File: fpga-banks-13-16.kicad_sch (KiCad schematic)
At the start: 40 parts, among them U14 XC7A100T-FGG484, U15 Oscillator_100MHz_AMJMEFB

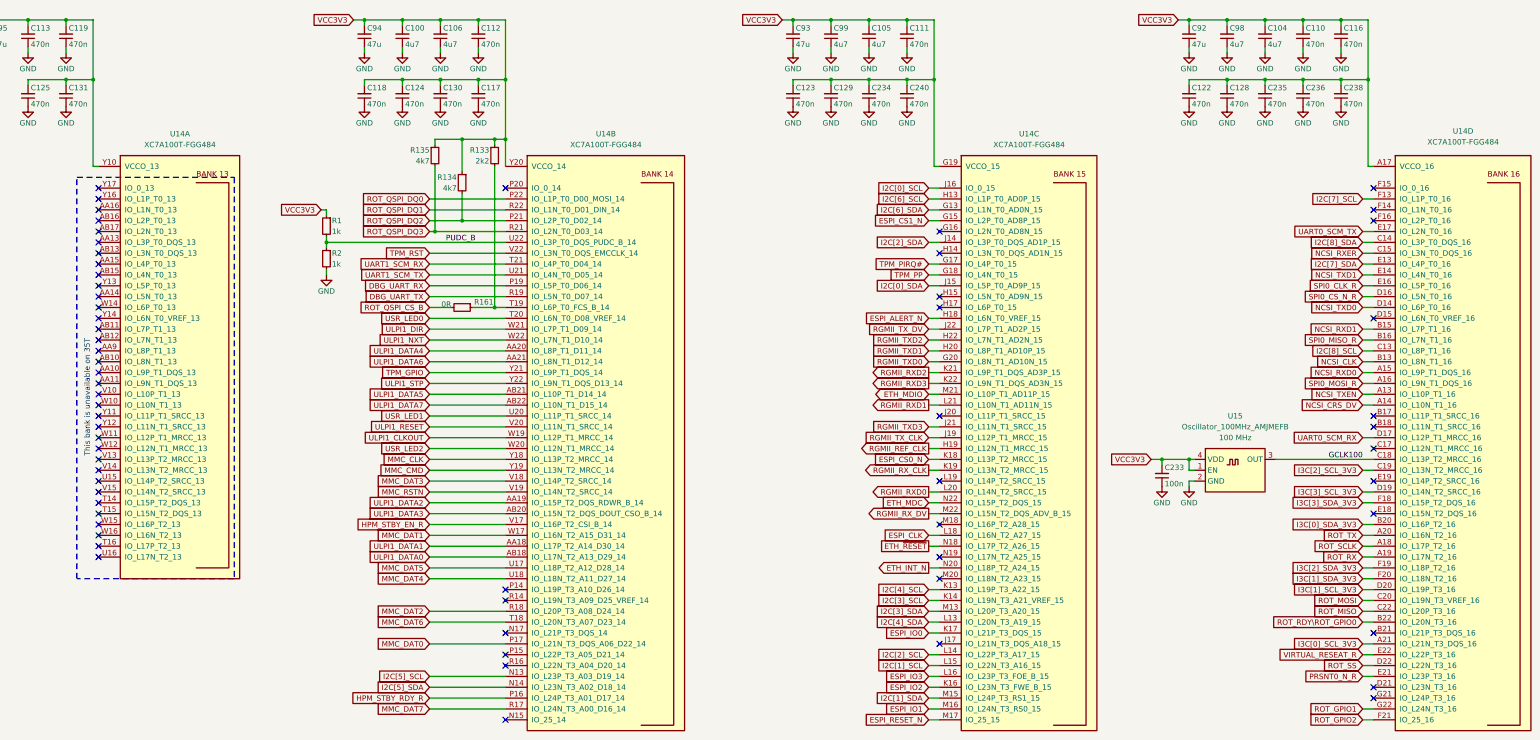
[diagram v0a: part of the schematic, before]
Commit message: [#68236] Update symbols and footprints, clean ERC and DRC
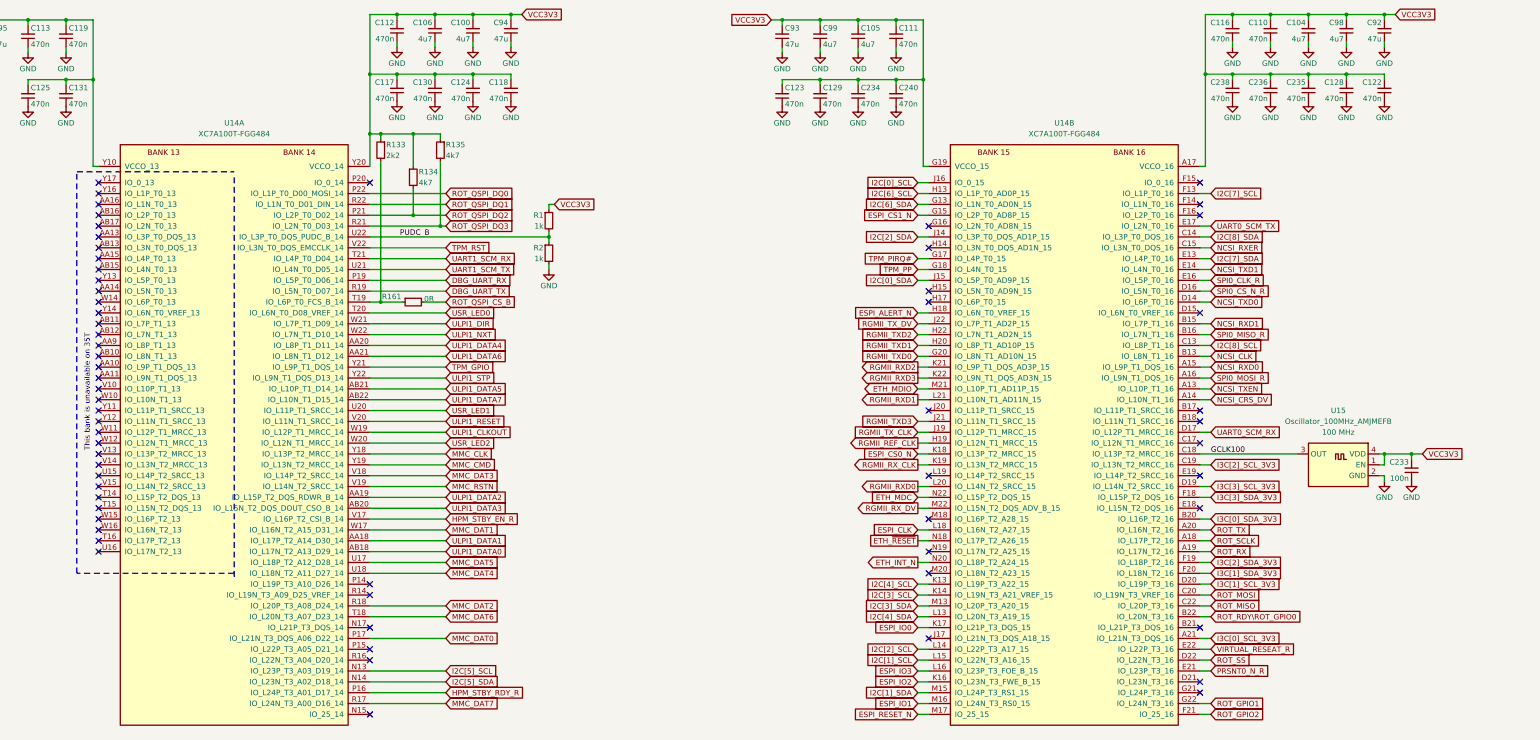
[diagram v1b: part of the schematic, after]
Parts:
- removed unit 3 of U14
- removed unit 4 of U14
- C92, C93, C94, C95: Public (none) -> False
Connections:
- net DBG_UART_RX: now also U14.P19 (IO_L5P_T0_D06_14); no longer U14.P19 (IO_L5P_T0_D06_14)
- net DBG_UART_TX: now also U14.R19 (IO_L5N_T0_D07_14); no longer U14.R19 (IO_L5N_T0_D07_14)
- net ESPI_ALERT_N: now also U14.H18 (IO_L6N_T0_VREF_15)
- net ESPI_CLK: now also U14.L18 (IO_L16N_T2_A27_15)
- net ESPI_CS0_N: now also U14.K18 (IO_L13P_T2_MRCC_15)
- net ESPI_CS1_N: now also U14.G15 (IO_L2P_T0_AD8P_15)
- net ESPI_IO0: now also U14.K17 (IO_L21P_T3_DQS_15)
- net ESPI_IO1: now also U14.M16 (IO_L24N_T3_RS0_15)
- net ESPI_IO2: now also U14.K16 (IO_L23N_T3_FWE_B_15)
- net ESPI_IO3: now also U14.L16 (IO_L23P_T3_FOE_B_15)
- net ESPI_RESET_N: now also U14.M17 (IO_25_15)
- net ETH_INT_N: now also U14.N20 (IO_L18P_T2_A24_15)
- net ETH_MDC: now also U14.N22 (IO_L15P_T2_DQS_15)
- net ETH_MDIO: now also U14.M21 (IO_L10P_T1_AD11P_15)
- net ETH_~{RESET}: now also U14.N18 (IO_L17P_T2_A26_15)
- net GCLK100: now also U14.C18 (IO_L13P_T2_MRCC_16)
- net HPM_STBY_EN_R: now also U14.V17 (IO_L16P_T2_CSI_B_14); no longer U14.V17 (IO_L16P_T2_CSI_B_14)
- net HPM_STBY_RDY_R: now also U14.P16 (IO_L24P_T3_A01_D17_14); no longer U14.P16 (IO_L24P_T3_A01_D17_14)
- net I2C[0]_SCL: now also U14.J16 (IO_0_15)
- net I2C[0]_SDA: now also U14.J15 (IO_L5P_T0_AD9P_15)
- net I2C[1]_SCL: now also U14.L15 (IO_L22N_T3_A16_15)
- net I2C[1]_SDA: now also U14.M15 (IO_L24P_T3_RS1_15)
- net I2C[2]_SCL: now also U14.L14 (IO_L22P_T3_A17_15)
- net I2C[2]_SDA: now also U14.J14 (IO_L3P_T0_DQS_AD1P_15)
- net I2C[3]_SCL: now also U14.K14 (IO_L19N_T3_A21_VREF_15)
- net I2C[3]_SDA: now also U14.M13 (IO_L20P_T3_A20_15)
- net I2C[4]_SCL: now also U14.K13 (IO_L19P_T3_A22_15)
- net I2C[4]_SDA: now also U14.L13 (IO_L20N_T3_A19_15)
- net I2C[5]_SCL: now also U14.N13 (IO_L23P_T3_A03_D19_14); no longer U14.N13 (IO_L23P_T3_A03_D19_14)
- net I2C[5]_SDA: now also U14.N14 (IO_L23N_T3_A02_D18_14); no longer U14.N14 (IO_L23N_T3_A02_D18_14)
- net I2C[6]_SCL: now also U14.H13 (IO_L1P_T0_AD0P_15)
- net I2C[6]_SDA: now also U14.G13 (IO_L1N_T0_AD0N_15)
- net I2C[7]_SCL: now also U14.F13 (IO_L1P_T0_16)
- net I2C[7]_SDA: now also U14.E13 (IO_L4P_T0_16)
- net I2C[8]_SCL: now also U14.C13 (IO_L8P_T1_16)
- net I2C[8]_SDA: now also U14.C14 (IO_L3P_T0_DQS_16)
- net I3C[0]_SCL_3V3: now also U14.A21 (IO_L21N_T3_DQS_16)
- net I3C[0]_SDA_3V3: now also U14.B20 (IO_L16P_T2_16)
- net I3C[1]_SCL_3V3: now also U14.D20 (IO_L19P_T3_16)
- net I3C[1]_SDA_3V3: now also U14.F20 (IO_L18N_T2_16)
- net I3C[2]_SCL_3V3: now also U14.C19 (IO_L13N_T2_MRCC_16)
- net I3C[2]_SDA_3V3: now also U14.F19 (IO_L18P_T2_16)
- net I3C[3]_SCL_3V3: now also U14.D19 (IO_L14N_T2_SRCC_16)
- net I3C[3]_SDA_3V3: now also U14.F18 (IO_L15P_T2_DQS_16)
- net MMC_CLK: now also U14.Y18 (IO_L13P_T2_MRCC_14); no longer U14.Y18 (IO_L13P_T2_MRCC_14)
- net MMC_CMD: now also U14.Y19 (IO_L13N_T2_MRCC_14); no longer U14.Y19 (IO_L13N_T2_MRCC_14)
- net MMC_DAT0: now also U14.P17 (IO_L21N_T3_DQS_A06_D22_14); no longer U14.P17 (IO_L21N_T3_DQS_A06_D22_14)
- net MMC_DAT1: now also U14.W17 (IO_L16N_T2_A15_D31_14); no longer U14.W17 (IO_L16N_T2_A15_D31_14)
- net MMC_DAT2: now also U14.R18 (IO_L20P_T3_A08_D24_14); no longer U14.R18 (IO_L20P_T3_A08_D24_14)
- net MMC_DAT3: now also U14.V18 (IO_L14P_T2_SRCC_14); no longer U14.V18 (IO_L14P_T2_SRCC_14)
- net MMC_DAT4: now also U14.U18 (IO_L18N_T2_A11_D27_14); no longer U14.U18 (IO_L18N_T2_A11_D27_14)
- net MMC_DAT5: now also U14.U17 (IO_L18P_T2_A12_D28_14); no longer U14.U17 (IO_L18P_T2_A12_D28_14)
- net MMC_DAT6: now also U14.T18 (IO_L20N_T3_A07_D23_14); no longer U14.T18 (IO_L20N_T3_A07_D23_14)
- net MMC_DAT7: now also U14.R17 (IO_L24N_T3_A00_D16_14); no longer U14.R17 (IO_L24N_T3_A00_D16_14)
- net MMC_RSTN: now also U14.V19 (IO_L14N_T2_SRCC_14); no longer U14.V19 (IO_L14N_T2_SRCC_14)
- net NCSI_CLK: now also U14.B13 (IO_L8N_T1_16)
- net NCSI_CRS_DV: now also U14.A14 (IO_L10N_T1_16)
- net NCSI_RXD0: now also U14.A15 (IO_L9P_T1_DQS_16)
- net NCSI_RXD1: now also U14.B15 (IO_L7P_T1_16)
- net NCSI_RXER: now also U14.C15 (IO_L3N_T0_DQS_16)
- net NCSI_TXD0: now also U14.D14 (IO_L6P_T0_16)
- net NCSI_TXD1: now also U14.E14 (IO_L4N_T0_16)
- net NCSI_TXEN: now also U14.A13 (IO_L10P_T1_16)
- net PRSNT0_N_R: now also U14.E21 (IO_L23P_T3_16)
- net PUDC_B: now also U14.U22 (IO_L3P_T0_DQS_PUDC_B_14); no longer U14.U22 (IO_L3P_T0_DQS_PUDC_B_14)
- net RGMII_REF_CLK: now also U14.H19 (IO_L12N_T1_MRCC_15)
- net RGMII_RXD0: now also U14.L20 (IO_L14N_T2_SRCC_15)
- net RGMII_RXD1: now also U14.L21 (IO_L10N_T1_AD11N_15)
- net RGMII_RXD2: now also U14.K21 (IO_L9P_T1_DQS_AD3P_15)
- net RGMII_RXD3: now also U14.K22 (IO_L9N_T1_DQS_AD3N_15)
- net RGMII_RX_CLK: now also U14.K19 (IO_L13N_T2_MRCC_15)
- net RGMII_RX_DV: now also U14.M22 (IO_L15N_T2_DQS_ADV_B_15)
- net RGMII_TXD0: now also U14.G20 (IO_L8N_T1_AD10N_15)
- net RGMII_TXD1: now also U14.H20 (IO_L8P_T1_AD10P_15)
- net RGMII_TXD2: now also U14.H22 (IO_L7N_T1_AD2N_15)
- net RGMII_TXD3: now also U14.J21 (IO_L11N_T1_SRCC_15)
- net RGMII_TX_CLK: now also U14.J19 (IO_L12P_T1_MRCC_15)
- net RGMII_TX_DV: now also U14.J22 (IO_L7P_T1_AD2P_15)
- net ROT_GPIO1: now also U14.G22 (IO_L24N_T3_16)
- net ROT_GPIO2: now also U14.F21 (IO_25_16)
- net ROT_MISO: now also U14.C22 (IO_L20P_T3_16)
- net ROT_MOSI: now also U14.C20 (IO_L19N_T3_VREF_16)
- net ROT_QSPI_DQ0: now also U14.P22 (IO_L1P_T0_D00_MOSI_14); no longer U14.P22 (IO_L1P_T0_D00_MOSI_14)
- net ROT_QSPI_DQ1: now also U14.R22 (IO_L1N_T0_D01_DIN_14); no longer U14.R22 (IO_L1N_T0_D01_DIN_14)
- net ROT_QSPI_DQ2: now also U14.P21 (IO_L2P_T0_D02_14); no longer U14.P21 (IO_L2P_T0_D02_14)
- net ROT_QSPI_DQ3: now also U14.R21 (IO_L2N_T0_D03_14); no longer U14.R21 (IO_L2N_T0_D03_14)
- net ROT_RDY\ROT_GPIO0: now also U14.B22 (IO_L20N_T3_16)
- net ROT_RX: now also U14.A19 (IO_L17N_T2_16)
- net ROT_SCLK: now also U14.A18 (IO_L17P_T2_16)
- net ROT_SS: now also U14.D22 (IO_L22N_T3_16)
- net ROT_TX: now also U14.A20 (IO_L16N_T2_16)
- net SPI0_CLK_R: now also U14.E16 (IO_L5P_T0_16)
- net SPI0_CS_N_R: now also U14.D16 (IO_L5N_T0_16)
- net SPI0_MISO_R: now also U14.B16 (IO_L7N_T1_16)
- net SPI0_MOSI_R: now also U14.A16 (IO_L9N_T1_DQS_16)
- net TPM_GPIO: now also U14.Y21 (IO_L9P_T1_DQS_14); no longer U14.Y21 (IO_L9P_T1_DQS_14)
- net TPM_PIRQ#: now also U14.G17 (IO_L4P_T0_15)
- net TPM_PP: now also U14.G18 (IO_L4N_T0_15)
- net TPM_RST: now also U14.V22 (IO_L3N_T0_DQS_EMCCLK_14); no longer U14.V22 (IO_L3N_T0_DQS_EMCCLK_14)
- net UART0_SCM_RX: now also U14.D17 (IO_L12P_T1_MRCC_16)
- net UART0_SCM_TX: now also U14.E17 (IO_L2N_T0_16)
- net UART1_SCM_RX: now also U14.T21 (IO_L4P_T0_D04_14); no longer U14.T21 (IO_L4P_T0_D04_14)
- net UART1_SCM_TX: now also U14.U21 (IO_L4N_T0_D05_14); no longer U14.U21 (IO_L4N_T0_D05_14)
- net ULPI1_CLKOUT: now also U14.W19 (IO_L12P_T1_MRCC_14); no longer U14.W19 (IO_L12P_T1_MRCC_14)
- net ULPI1_DATA0: now also U14.AB18 (IO_L17N_T2_A13_D29_14); no longer U14.AB18 (IO_L17N_T2_A13_D29_14)
- net ULPI1_DATA1: now also U14.AA18 (IO_L17P_T2_A14_D30_14); no longer U14.AA18 (IO_L17P_T2_A14_D30_14)
- net ULPI1_DATA2: now also U14.AA19 (IO_L15P_T2_DQS_RDWR_B_14); no longer U14.AA19 (IO_L15P_T2_DQS_RDWR_B_14)
- net ULPI1_DATA3: now also U14.AB20 (IO_L15N_T2_DQS_DOUT_CSO_B_14); no longer U14.AB20 (IO_L15N_T2_DQS_DOUT_CSO_B_14)
- net ULPI1_DATA4: now also U14.AA20 (IO_L8P_T1_D11_14); no longer U14.AA20 (IO_L8P_T1_D11_14)
- net ULPI1_DATA5: now also U14.AB21 (IO_L10P_T1_D14_14); no longer U14.AB21 (IO_L10P_T1_D14_14)
- net ULPI1_DATA6: now also U14.AA21 (IO_L8N_T1_D12_14); no longer U14.AA21 (IO_L8N_T1_D12_14)
- net ULPI1_DATA7: now also U14.AB22 (IO_L10N_T1_D15_14); no longer U14.AB22 (IO_L10N_T1_D15_14)
- net ULPI1_DIR: now also U14.W21 (IO_L7P_T1_D09_14); no longer U14.W21 (IO_L7P_T1_D09_14)
- net ULPI1_NXT: now also U14.W22 (IO_L7N_T1_D10_14); no longer U14.W22 (IO_L7N_T1_D10_14)
- net ULPI1_RESET: now also U14.V20 (IO_L11N_T1_SRCC_14); no longer U14.V20 (IO_L11N_T1_SRCC_14)
- net ULPI1_STP: now also U14.Y22 (IO_L9N_T1_DQS_D13_14); no longer U14.Y22 (IO_L9N_T1_DQS_D13_14)
- net USR_LED0: now also U14.T20 (IO_L6N_T0_D08_VREF_14); no longer U14.T20 (IO_L6N_T0_D08_VREF_14)
- net USR_LED1: now also U14.U20 (IO_L11P_T1_SRCC_14); no longer U14.U20 (IO_L11P_T1_SRCC_14)
- net USR_LED2: now also U14.W20 (IO_L12N_T1_MRCC_14); no longer U14.W20 (IO_L12N_T1_MRCC_14)
- net VCC3V3: now also U14.A17 (VCCO_16), U14.B14 (VCCO_16), U14.C21 (VCCO_16), U14.D18 (VCCO_16), U14.E15 (VCCO_16), U14.F22 (VCCO_16), U14.G19 (VCCO_15), U14.H16 (VCCO_15), U14.J13 (VCCO_15), U14.K20 (VCCO_15), U14.L17 (VCCO_15), U14.M14 (VCCO_14), U14.N21 (VCCO_15), U14.P18 (VCCO_14), U14.R15 (VCCO_14), U14.T22 (VCCO_14), U14.U19 (VCCO_14), U14.Y20 (VCCO_14); no longer U14.M14 (VCCO_14), U14.P18 (VCCO_14), U14.R15 (VCCO_14), U14.T22 (VCCO_14), U14.U19 (VCCO_14), U14.Y20 (VCCO_14)
- net VIRTUAL_RESEAT_R: now also U14.E22 (IO_L22P_T3_16)
- net at R133.2, R161.1: now also U14.T19 (IO_L6P_T0_FCS_B_14); no longer U14.T19 (IO_L6P_T0_FCS_B_14)
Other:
- moved on the sheet: C105, C111, C123, C129, C234, C240, C93, C99

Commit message: pcb layout progress
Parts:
- added R204, R205, R206, R207, R208, R209: 33, Resistor_SMD:R_0402_1005Metric, symbol Device:R_Small
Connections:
- net RGMII_RXD0: now also R208.1; no longer U14.L20 (IO_L14N_T2_SRCC_15)
- net RGMII_RXD1: now also R206.1; no longer U14.L21 (IO_L10N_T1_AD11N_15)
- net RGMII_RXD2: now also R204.1; no longer U14.K21 (IO_L9P_T1_DQS_AD3P_15)
- net RGMII_RXD3: now also R205.1; no longer U14.K22 (IO_L9N_T1_DQS_AD3N_15)
- net RGMII_RX_CLK: now also R207.1; no longer U14.K19 (IO_L13N_T2_MRCC_15)
- net RGMII_RX_DV: now also R209.1; no longer U14.M22 (IO_L15N_T2_DQS_ADV_B_15)
- new net RGMII_CLK_FPGA: R207.2, U14.K19 (IO_L13N_T2_MRCC_15)
- new net RGMII_RXD0_FPGA: R208.2, U14.L20 (IO_L14N_T2_SRCC_15)
- new net RGMII_RXD1_FPGA: R206.2, U14.L21 (IO_L10N_T1_AD11N_15)
- new net RGMII_RXD2_FPGA: R204.2, U14.K21 (IO_L9P_T1_DQS_AD3P_15)
- new net RGMII_RXD3_FPGA: R205.2, U14.K22 (IO_L9N_T1_DQS_AD3N_15)
- new net RGMII_RX_DV_FPGA: R209.2, U14.M22 (IO_L15N_T2_DQS_ADV_B_15)

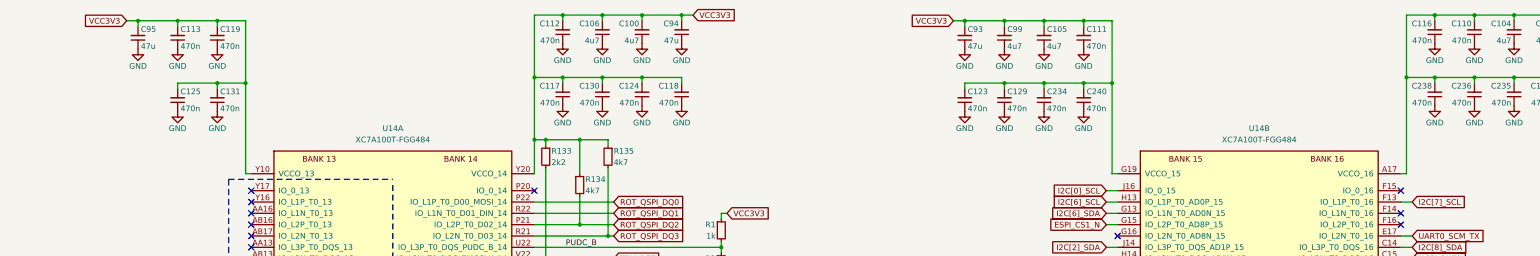
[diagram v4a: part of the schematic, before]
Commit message: a lot of routing and almost all caps of the fpga are placed down
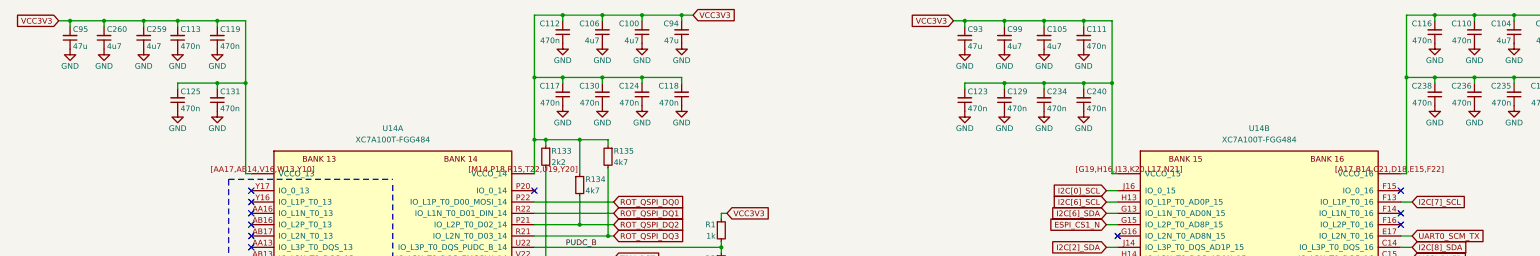
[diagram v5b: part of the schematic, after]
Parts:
- added C259, C260: C_4u7_0603, Capacitor_SMD:C_0603_1608Metric, symbol antmicroCapacitors0603:C_4u7_0603
- C100, C104, C105, C106, C98, C99: footprint antmicro-footprints:C_0603_1608Metric -> Capacitor_SMD:C_0603_1608Metric; MPN C1608X5R1V475M080AC -> C0603C475K9PAC; Manufacturer TDK -> KEMET
- C110, C111, C112, C113, C116, C117, C118, C119, C122, C123, C124, C125, C128, C129, C130, C131, C233, C234, C235, C236, C238, C240: footprint antmicro-footprints:C_0402_1005Metric -> Capacitor_SMD:C_0402_1005Metric
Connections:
- net GND: now also C259.1, C260.1
- net VCC3V3: now also U14.[A17,B14,C21,D18,E15,F22] (VCCO_16), U14.[AA17,AB14,V16,W13,Y10] (VCCO_13), U14.[G19,H16,J13,K20,L17,N21] (VCCO_15), U14.[M14,P18,R15,T22,U19,Y20] (VCCO_14), C259.2, C260.2; no longer U14.A17 (VCCO_16), U14.AA17 (VCCO_13), U14.AB14 (VCCO_13), U14.B14 (VCCO_16), U14.C21 (VCCO_16), U14.D18 (VCCO_16), U14.E15 (VCCO_16), U14.F22 (VCCO_16), U14.G19 (VCCO_15), U14.H16 (VCCO_15), U14.J13 (VCCO_15), U14.K20 (VCCO_15), U14.L17 (VCCO_15), U14.M14 (VCCO_14), U14.N21 (VCCO_15), U14.P18 (VCCO_14), U14.R15 (VCCO_14), U14.T22 (VCCO_14), U14.U19 (VCCO_14), U14.V16 (VCCO_13), U14.W13 (VCCO_13), U14.Y10 (VCCO_13), U14.Y20 (VCCO_14)
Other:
- moved on the sheet: C95, U14A

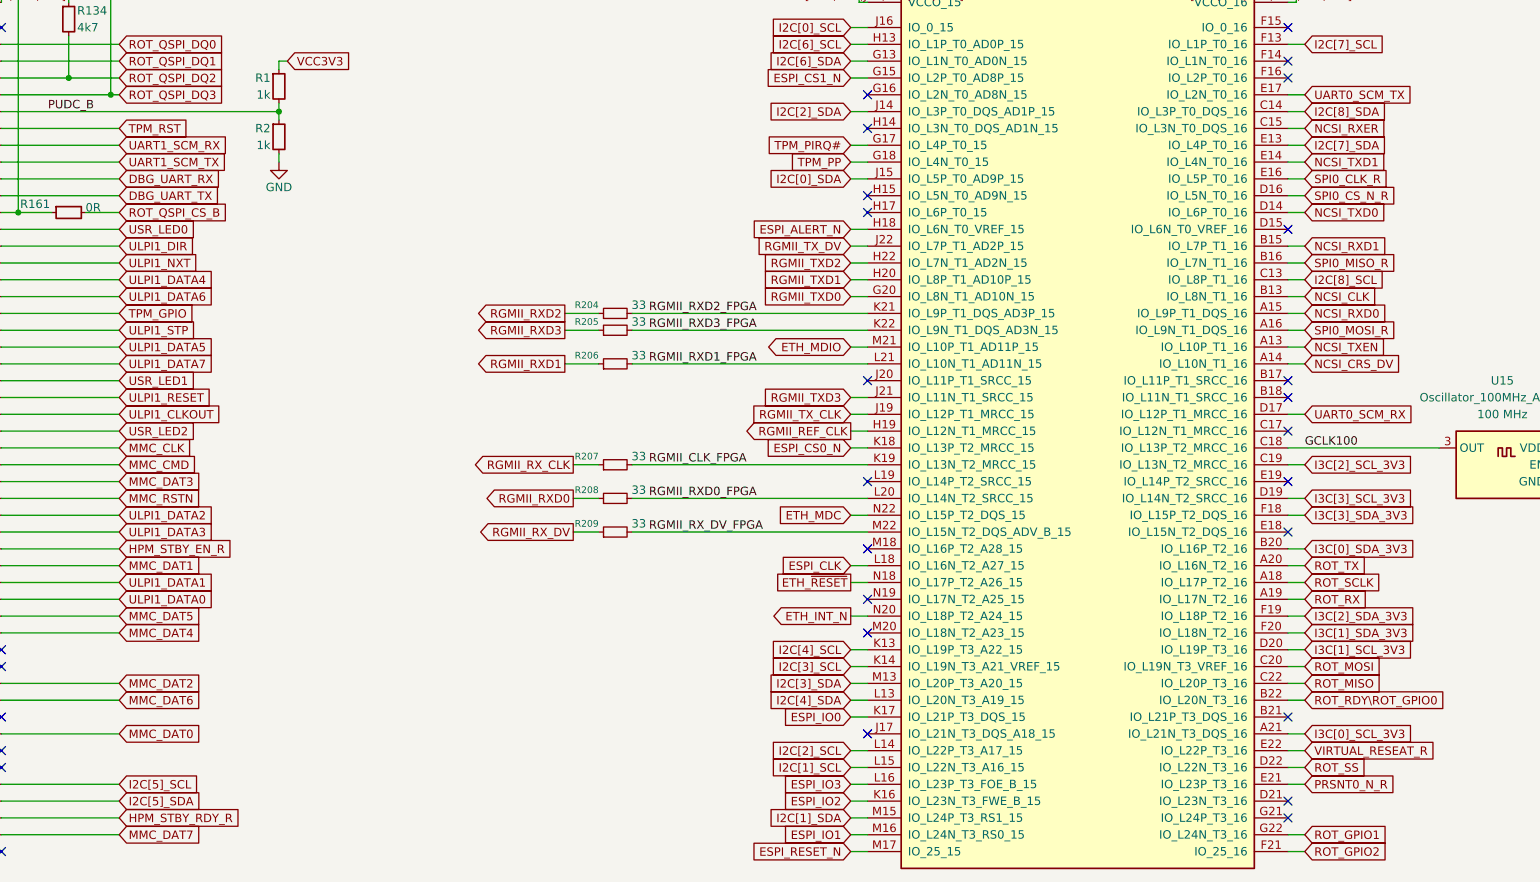
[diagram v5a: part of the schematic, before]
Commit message: a lot of poin swaps
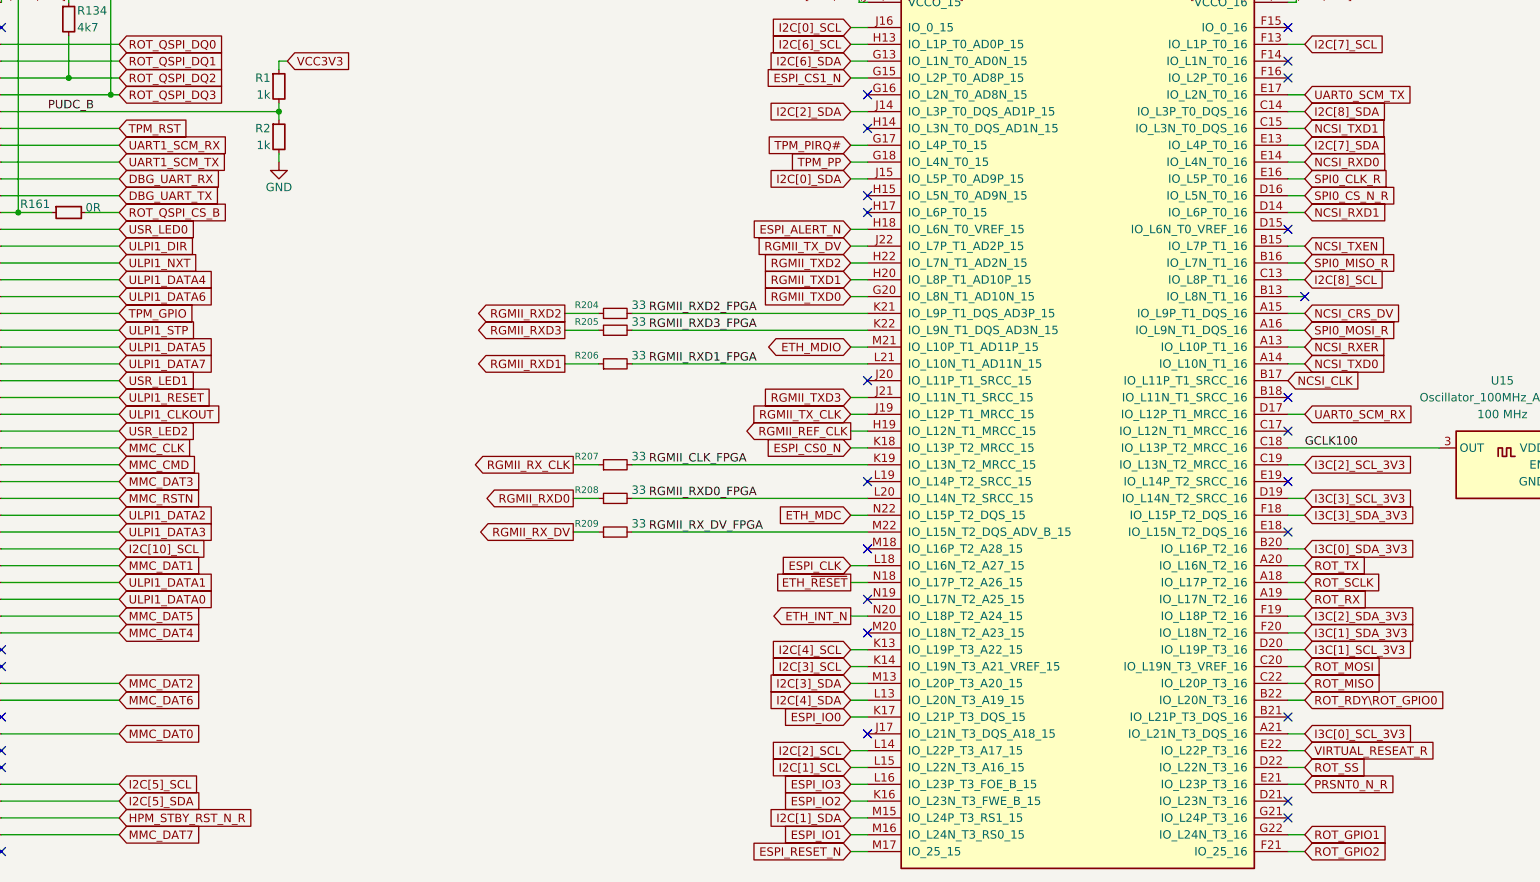
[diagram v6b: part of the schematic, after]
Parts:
- C110, C111, C112, C113, C116, C117, C118, C119, C122, C123, C124, C125, C128, C129, C130, C131, C234, C235, C236, C238, C240: MPN C1005X5R1E474M050BB -> GXT155C80J474KE01D; Manufacturer TDK -> Murata Electronics
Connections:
- net NCSI_CLK: now also U14.B17 (IO_L11P_T1_SRCC_16); no longer U14.B13 (IO_L8N_T1_16)
- net NCSI_CRS_DV: now also U14.A15 (IO_L9P_T1_DQS_16); no longer U14.A14 (IO_L10N_T1_16)
- net NCSI_RXD0: now also U14.E14 (IO_L4N_T0_16); no longer U14.A15 (IO_L9P_T1_DQS_16)
- net NCSI_RXD1: now also U14.D14 (IO_L6P_T0_16); no longer U14.B15 (IO_L7P_T1_16)
- net NCSI_RXER: now also U14.A13 (IO_L10P_T1_16); no longer U14.C15 (IO_L3N_T0_DQS_16)
- net NCSI_TXD0: now also U14.A14 (IO_L10N_T1_16); no longer U14.D14 (IO_L6P_T0_16)
- net NCSI_TXD1: now also U14.C15 (IO_L3N_T0_DQS_16); no longer U14.E14 (IO_L4N_T0_16)
- net NCSI_TXEN: now also U14.B15 (IO_L7P_T1_16); no longer U14.A13 (IO_L10P_T1_16)
- net HPM_STBY_EN_R renamed I2C[10]_SCL
- net HPM_STBY_RDY_R renamed HPM_STBY_RST_N_R

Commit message: river routing
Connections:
- net ESPI_ALERT_N: now also U14.D16 (IO_L5N_T0_16); no longer U14.H18 (IO_L6N_T0_VREF_15)
- net ESPI_CLK: now also U14.D17 (IO_L12P_T1_MRCC_16); no longer U14.L18 (IO_L16N_T2_A27_15)
- net ESPI_CS0_N: now also U14.E16 (IO_L5P_T0_16); no longer U14.K18 (IO_L13P_T2_MRCC_15)
- net ESPI_CS1_N: now also U14.H13 (IO_L1P_T0_AD0P_15); no longer U14.G15 (IO_L2P_T0_AD8P_15)
- net ESPI_IO0: now also U14.C14 (IO_L3P_T0_DQS_16); no longer U14.K17 (IO_L21P_T3_DQS_15)
- net ESPI_IO1: now also U14.E13 (IO_L4P_T0_16); no longer U14.M16 (IO_L24N_T3_RS0_15)
- net ESPI_IO2: now also U14.E17 (IO_L2N_T0_16); no longer U14.K16 (IO_L23N_T3_FWE_B_15)
- net ESPI_IO3: now also U14.F13 (IO_L1P_T0_16); no longer U14.L16 (IO_L23P_T3_FOE_B_15)
- net ESPI_RESET_N: now also U14.G13 (IO_L1N_T0_AD0N_15); no longer U14.M17 (IO_25_15)
- net I2C[6]_SCL: now also U14.G15 (IO_L2P_T0_AD8P_15); no longer U14.H13 (IO_L1P_T0_AD0P_15)
- net I2C[6]_SDA: now also U14.M17 (IO_25_15); no longer U14.G13 (IO_L1N_T0_AD0N_15)
- net I2C[7]_SCL: now also U14.L16 (IO_L23P_T3_FOE_B_15); no longer U14.F13 (IO_L1P_T0_16)
- net I2C[7]_SDA: now also U14.M16 (IO_L24N_T3_RS0_15); no longer U14.E13 (IO_L4P_T0_16)
- net I2C[8]_SDA: now also U14.K17 (IO_L21P_T3_DQS_15); no longer U14.C14 (IO_L3P_T0_DQS_16)
- net SPI0_CLK_R: now also U14.K18 (IO_L13P_T2_MRCC_15); no longer U14.E16 (IO_L5P_T0_16)
- net SPI0_CS_N_R: now also U14.H18 (IO_L6N_T0_VREF_15); no longer U14.D16 (IO_L5N_T0_16)
- net UART0_SCM_RX: now also U14.L18 (IO_L16N_T2_A27_15); no longer U14.D17 (IO_L12P_T1_MRCC_16)
- net UART0_SCM_TX: now also U14.K16 (IO_L23N_T3_FWE_B_15); no longer U14.E17 (IO_L2N_T0_16)
- net HPM_STBY_RST_N_R renamed SGPIO0_DI
